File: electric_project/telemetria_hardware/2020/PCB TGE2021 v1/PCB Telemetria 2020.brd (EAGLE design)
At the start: 160 x 100 mm, 4 parts, among them IC1 INA240A1DR

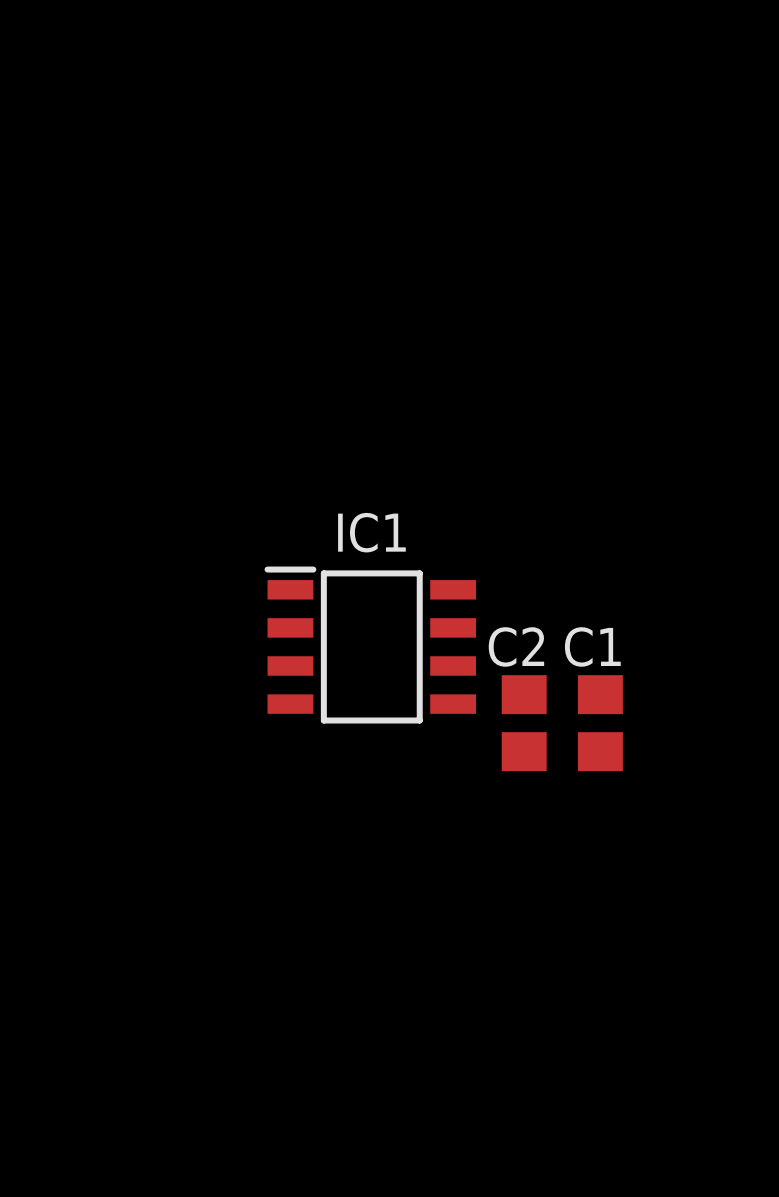
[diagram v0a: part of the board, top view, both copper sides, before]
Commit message: Att shunt measure and organizing folders
Some folders organized and RC filter added to the motor shunt measure
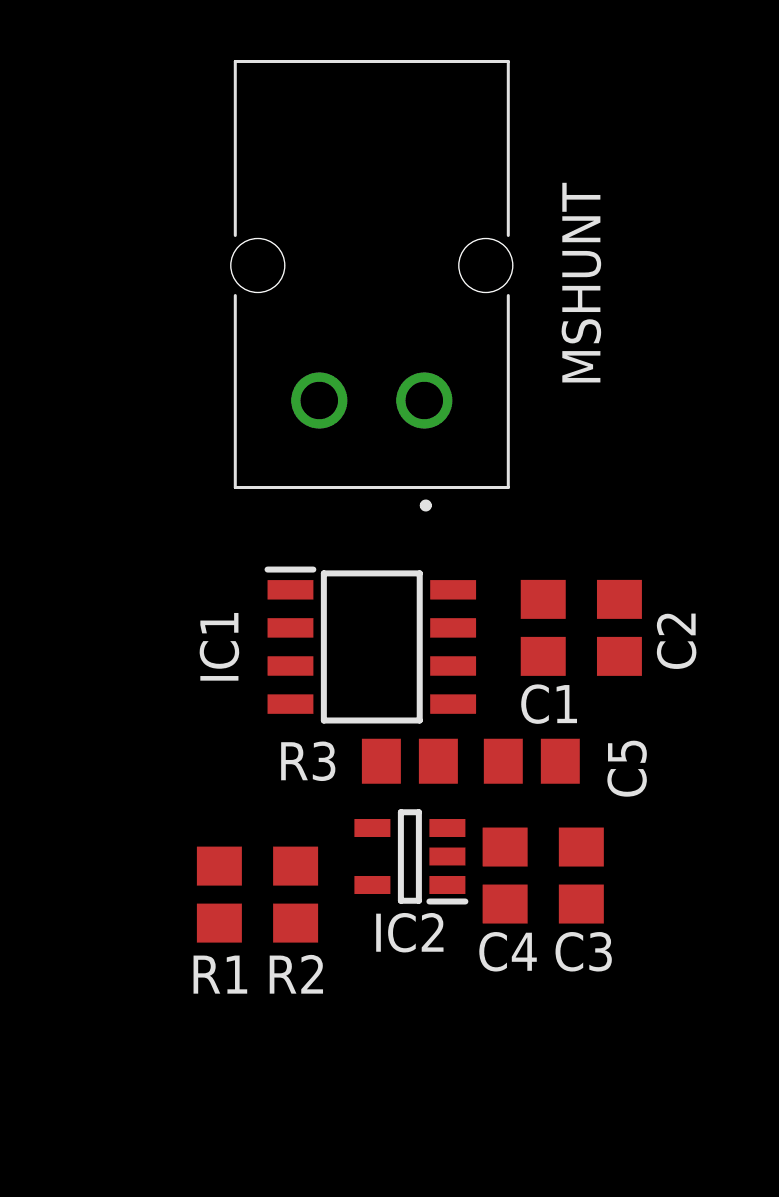
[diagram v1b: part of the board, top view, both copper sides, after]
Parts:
- added C3: 10uF, rcl:C0805
- added C4, C5: 100nF, rcl:C0805
- added IC2: MCP3221A6T-E_OTVAO, MCP3221A6T-E_OTVAO:SOT95P280X145-5N
- added MSHUNT: 53259-0229, CON_MOLEX_53259-0229:0532590229
- added R1, R2: (no value), rcl:R0805
- added R3: 680R, rcl:R0805
- moved C2 4.49 mm to (193.7, 97.2), turned to 90 degrees
- moved C1 3.70 mm to (191.1, 97.2), turned to 90 degrees
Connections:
- new net I2C_SCL: IC2.5, R2.1, U$1.21
- new net I2C_SDA: IC2.4, R1.1, U$1.22
- new net MSHUNT_ADC: C5.1, IC2.3, R3.1
- new net MSHUNT_AMP: IC1.5, R3.2
- new net N$10: U$1.25
- new net N$11: U$1.14
- new net N$12: U$1.13
- new net N$13: U$1.2
- new net N$15: U$1.5V
- new net N$16: U$1.TX
- new net N$17: U$1.RX
- new net N$18: U$1.23
- new net N$19: U$1.4
- new net N$20: U$1.0
- new net N$23: U$1.GND1
- new net N$27: U$1.LORA2
- new net N$28: U$1.LORA1
- new net N$3: U$1.VP
- new net N$4: U$1.VN
- new net N$5: U$1.RST
- new net N$6: U$1.34
- new net N$7: U$1.35
- new net N$9: U$1.33
- net GND: now also C3.2, C4.2, C5.2, IC2.2, U$1.GND, U$1.GND3
- net MSHUNT_N: now also MSHUNT.2
- net MSHUNT_P: now also MSHUNT.1
- net N$8: now also U$1.32; no longer IC1.5
- net VCC_3V3: now also C3.1, C4.1, IC2.1, R1.2, R2.2, U$1.3.3V, U$1.3V3

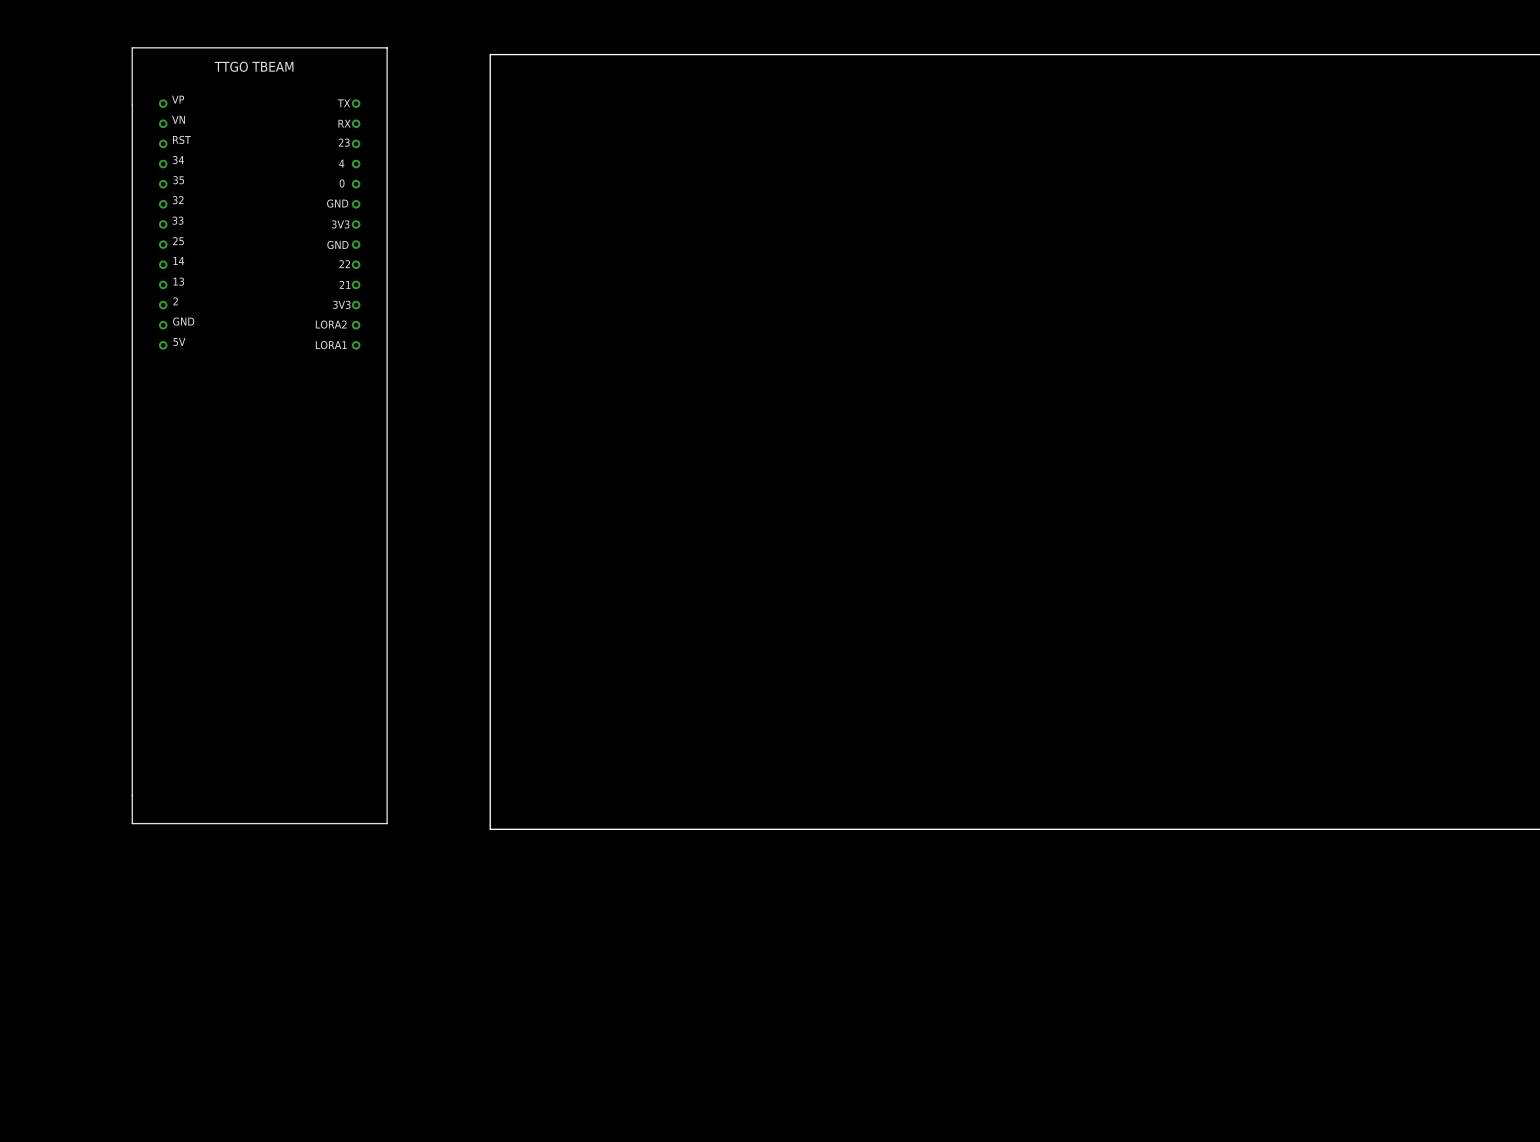
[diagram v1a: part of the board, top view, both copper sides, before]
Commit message: Begining of 3V3 Regulator Circuit
LDO AZ111 added to the circuit. The input filter is under research.
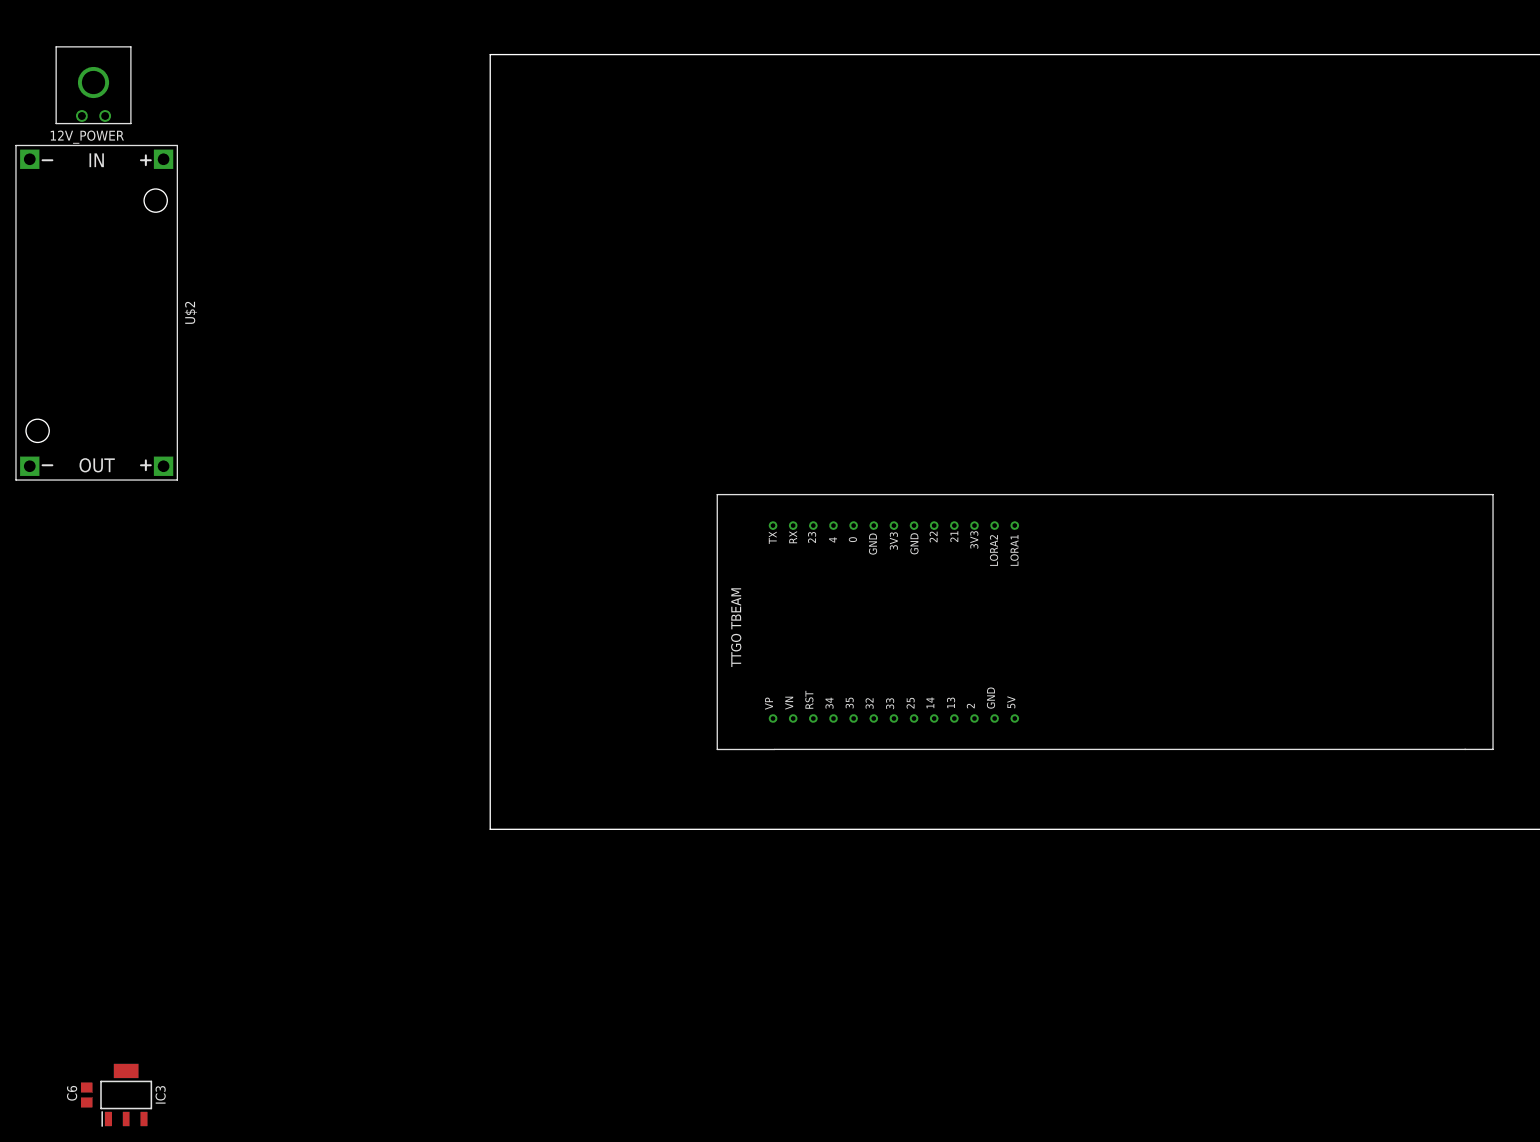
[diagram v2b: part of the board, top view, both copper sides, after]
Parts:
- added 12V_POWER: 43650-0200, 43650-0200:43650-0200
- added C6: 100nF, rcl:C0805
- added IC3: AZ1117IH-3.3TRG1, AZ1117IH-3.3TRG1:SOT230P700X170-4N
- added U$2: DC-DC-STEP-DOWN-LM2596, diy-modules:DC-DC-STEP-DOWN-LM2596
- moved U$1 96.1 mm to (52.7, 27.3), turned to 90 degrees
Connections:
- new net VCC_12V: 12V_POWER.2, U$2.IN+
- new net VCC_5V: IC3.3, U$2.OUT+
- net GND: now also 12V_POWER.1, C6.2, IC3.1, U$2.IN-, U$2.OUT-
- net VCC_3V3: now also C6.1, IC3.2, IC3.4

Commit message: apenas corrigi o valor de um capacitor
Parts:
- C6: value 100nF -> 22uF
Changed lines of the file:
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@@
 <attribute name="VALUE" x="-46.99" y="-34.29" size="1.27" layer="27" rot="R90" align="center"/>
 </element>
-<element name="C6" library="rcl" library_urn="urn:adsk.eagle:library:334" package="C0805" package3d_urn="urn:adsk.eagle:package:23617/2" value="100nF" x="-52.07" y="-34.29" smashed="yes" rot="R270">
+<element name="C6" library="rcl" library_urn="urn:adsk.eagle:library:334" package="C0805" package3d_urn="urn:adsk.eagle:package:23617/2" value="22uF" x="-52.07" y="-34.29" smashed="yes" rot="R270">
 <attribute name="NAME" x="-54.61" y="-33.02" size="1.27" layer="25" rot="R270"/>
 <attribute name="POPULARITY" value="63" x="-52.07" y="-34.29" size="1.778" layer="27" rot="R270" display="off"/>
